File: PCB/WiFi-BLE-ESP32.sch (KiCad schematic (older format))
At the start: 27 parts, among them T1 1909763-1, U4 ESP32, U5 W25Q64FWSSIG, X3 FA-128_26.0000MF10Z-AC3

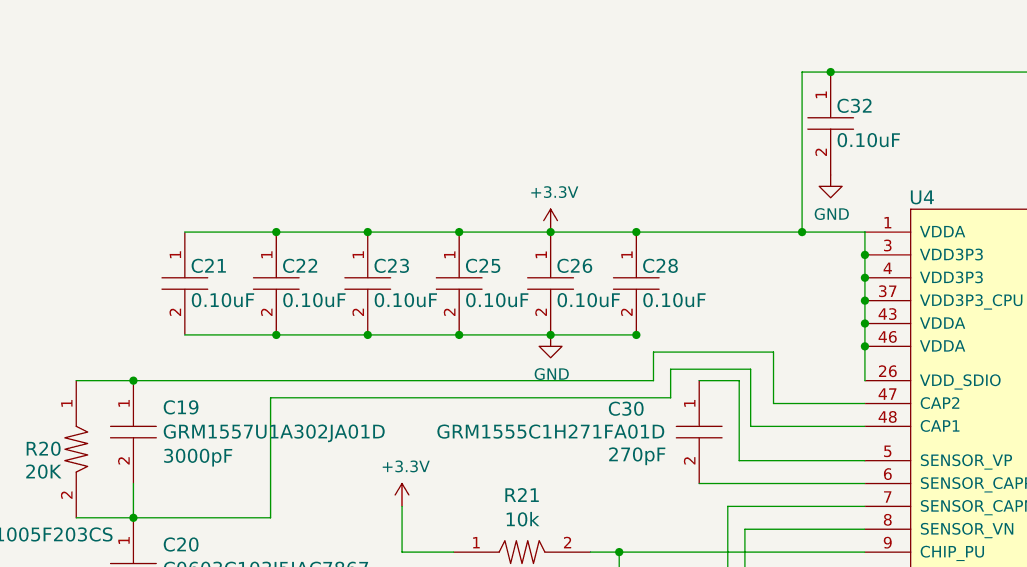
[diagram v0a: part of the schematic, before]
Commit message: Tweaking and ESP3212 version
Continuing to tweak the PCB, for optimal RF performance, thinking about
capping either the RF section of the MCU+RF entirely. Also made an
ESP3212 module version, both will be built at the same time when the
time comes.
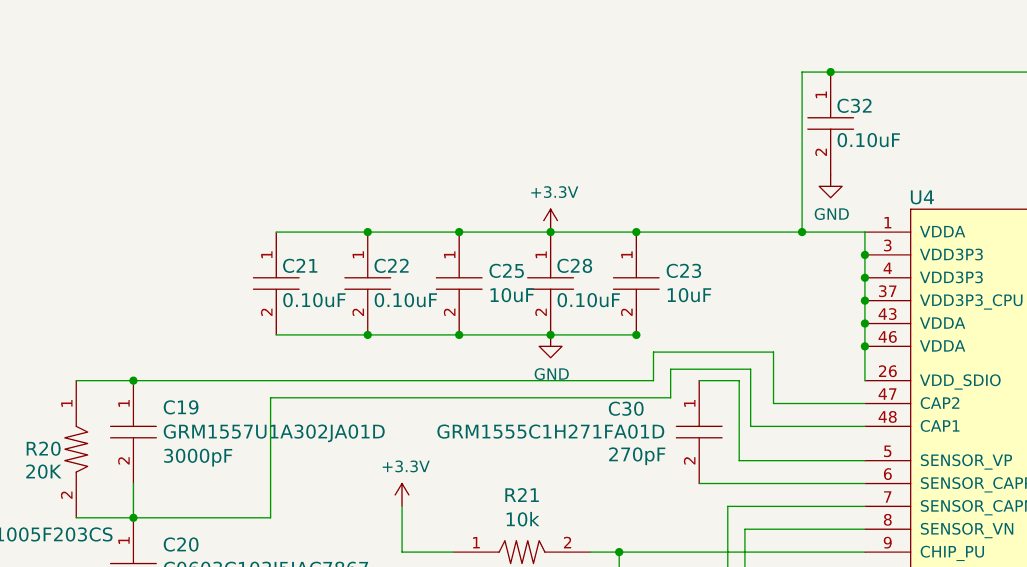
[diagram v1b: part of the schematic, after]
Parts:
- removed C23, C25, C26: CL05B104JP5NNNC, PCB_Footprints:C0402, symbol CL05B104JP5NNNC
- added C23, C25: CL10A106KQ8NNNC, PCB_Footprints:C0603, symbol CL10A106KQ8NNNC
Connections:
- net +3V3: now also C23.1, C25.1
- net GND: now also C23.2, C25.2
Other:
- moved on the sheet: C21, C22, C28

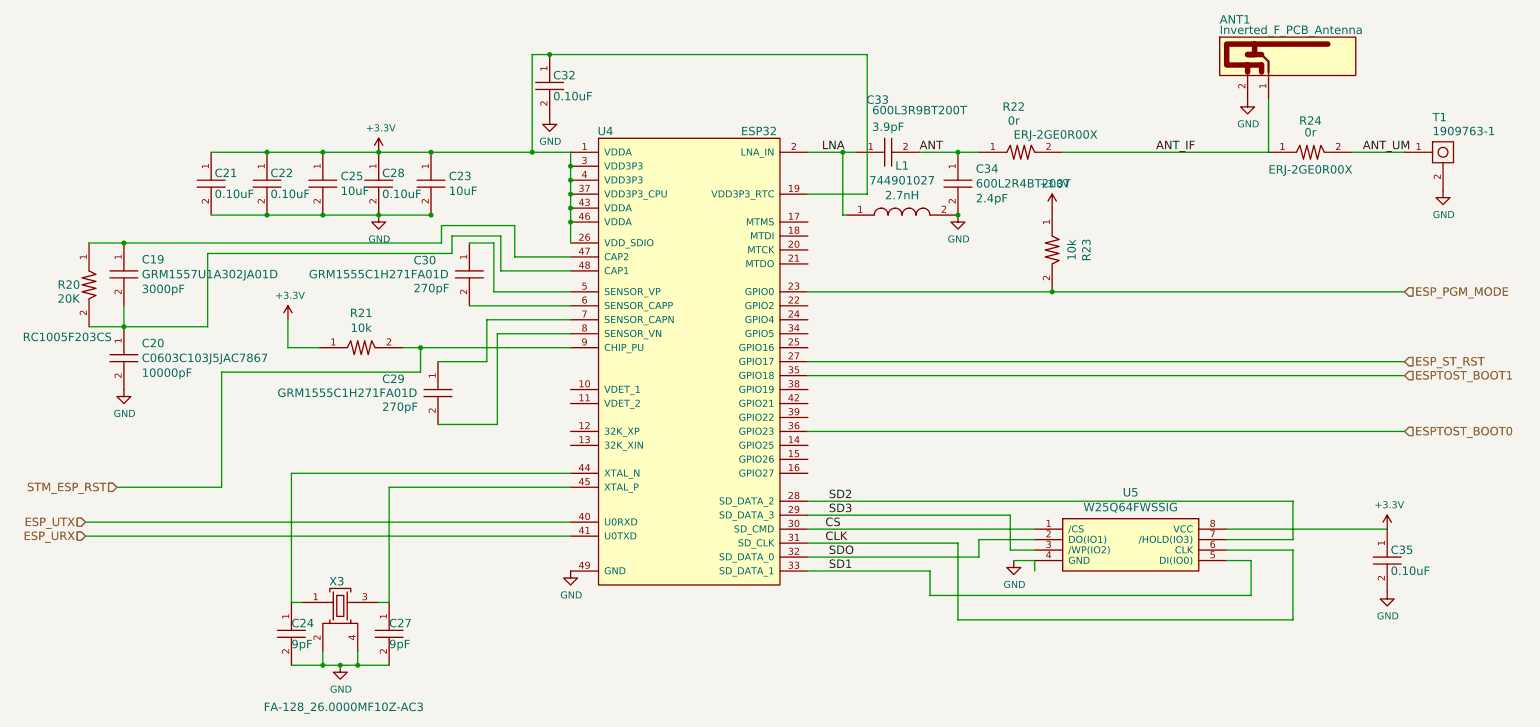
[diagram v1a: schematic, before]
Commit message: Tweaks, DRC cleared, images, readme
Tweaked both designs according to the dev board scheamtics provided by
Espressif in the datasheets folder. Cleared both boards of DRC
violations, added new images and updated the readme.
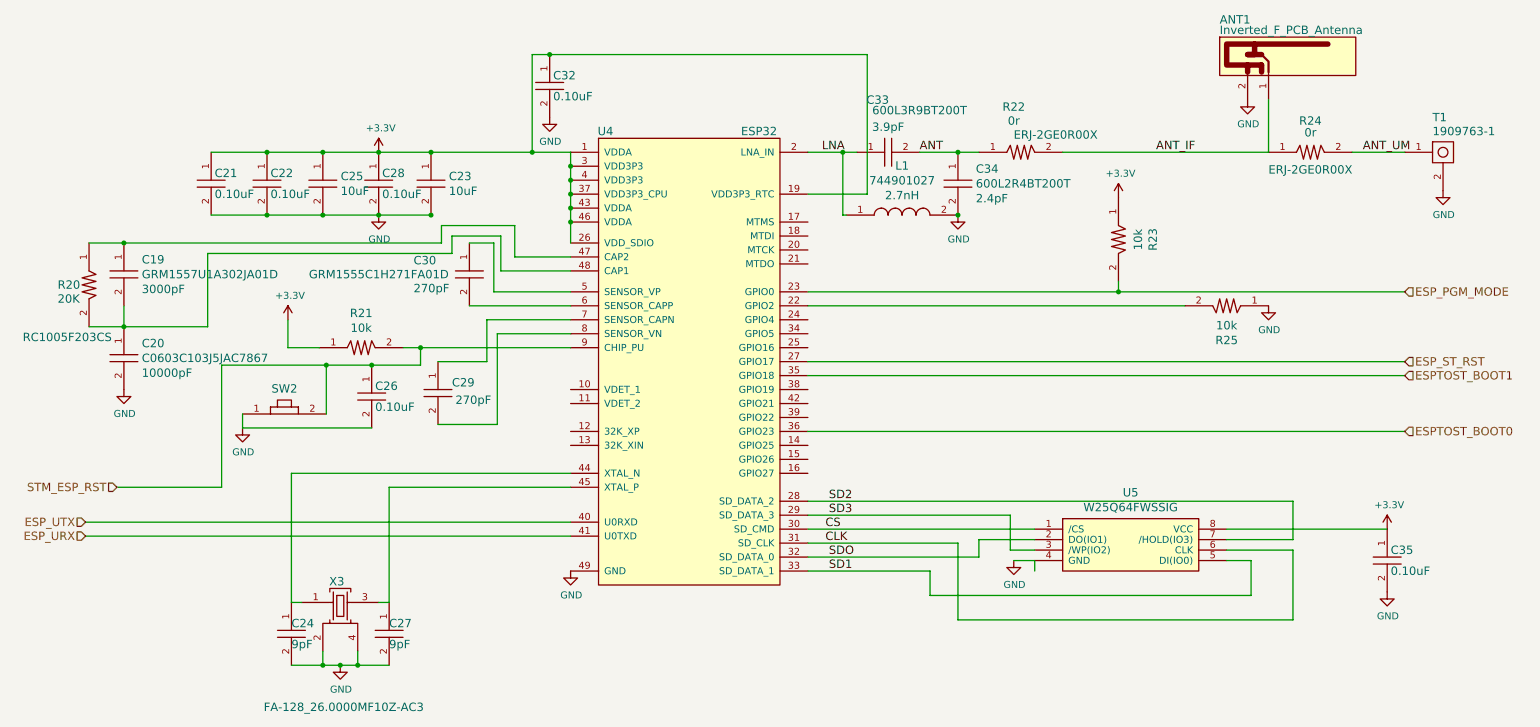
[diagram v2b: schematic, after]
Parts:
- added C26: CL05B104JP5NNNC, PCB_Footprints:C0402, symbol CL05B104JP5NNNC
- added R25: RC1005F103CS, PCB_Footprints:R0402, symbol RC1005F103CS
- added SW2: B3U-1000P, PCB_Footprints:B3U-1000P, symbol B3U-1000P
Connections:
- net GND: now also C26.2, R25.1, SW2.1
- net STM_ESP_RST: now also C26.1, SW2.2
- net at U4.22 (GPIO2): now also R25.2
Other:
- moved on the sheet: R23

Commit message: On/Off And Cleanup
Onoff Switch added, PCB extended 1mm to accomodated everything. routing
and traes cleaned up. Heat sinking ground pours added to the BQ chip
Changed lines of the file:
@@
 $EndComp
 $Comp
-L +3.3V #PWR40
+L +3.3V #PWR41
 U 1 1 57EA49BD
 P 3075 1950
-F 0 "#PWR40" H 3075 1800 50  0001 C CNN
+F 0 "#PWR41" H 3075 1800 50  0001 C CNN
 F 1 "+3.3V" H 3090 2123 50  0000 C CNN
 F 2 "" H 3075 1950 50  0000 C CNN
@@
 $EndComp
 $Comp
-L GND #PWR41
+L GND #PWR42
 U 1 1 57EA49DF
 P 3075 2400
-F 0 "#PWR41" H 3075 2150 50  0001 C CNN
+F 0 "#PWR42" H 3075 2150 50  0001 C CNN
 F 1 "GND" H 3080 2227 50  0000 C CNN
 F 2 "" H 3075 2400 50  0000 C CNN
@@
 $EndComp
 $Comp
-L GND #PWR43
+L GND #PWR44
 U 1 1 57EA4CD5
 P 4450 4950
-F 0 "#PWR43" H 4450 4700 50  0001 C CNN
+F 0 "#PWR44" H 4450 4700 50  0001 C CNN
 F 1 "GND" H 4455 4777 50  0000 C CNN
 F 2 "" H 4450 4950 50  0000 C CNN
@@
 $EndComp
 $Comp
-L +3.3V #PWR38
+L +3.3V #PWR39
 U 1 1 57EA52FC
 P 2425 3150
-F 0 "#PWR38" H 2425 3000 50  0001 C CNN
+F 0 "#PWR39" H 2425 3000 50  0001 C CNN
 F 1 "+3.3V" H 2440 3323 50  0000 C CNN
 F 2 "" H 2425 3150 50  0000 C CNN
@@
 $EndComp
 $Comp
-L GND #PWR39
+L GND #PWR40
 U 1 1 57EA84FC
 P 2800 5625
-F 0 "#PWR39" H 2800 5375 50  0001 C CNN
+F 0 "#PWR40" H 2800 5375 50  0001 C CNN
 F 1 "GND" H 2805 5452 50  0000 C CNN
 F 2 "" H 2800 5625 50  0000 C CNN
@@
 $EndComp
 $Comp
-L +3.3V #PWR46
+L +3.3V #PWR47
 U 1 1 5800AB01
 P 8375 2275
-F 0 "#PWR46" H 8375 2125 50  0001 C CNN
+F 0 "#PWR47" H 8375 2125 50  0001 C CNN
 F 1 "+3.3V" H 8390 2448 50  0000 C CNN
 F 2 "" H 8375 2275 50  0000 C CNN
@@
 $EndComp
 $Comp
-L +3.3V #PWR49
+L +3.3V #PWR50
 U 1 1 5800EACB
 P 10300 4650
-F 0 "#PWR49" H 10300 4500 50  0001 C CNN
+F 0 "#PWR50" H 10300 4500 50  0001 C CNN
 F 1 "+3.3V" H 10315 4823 50  0000 C CNN
 F 2 "" H 10300 4650 50  0000 C CNN
@@
 $EndComp
 $Comp
-L GND #PWR50
+L GND #PWR51
 U 1 1 5800EB03
 P 10300 5100
-F 0 "#PWR50" H 10300 4850 50  0001 C CNN
+F 0 "#PWR51" H 10300 4850 50  0001 C CNN
 F 1 "GND" H 10305 4927 50  0000 C CNN
 F 2 "" H 10300 5100 50  0000 C CNN
@@
 $EndComp
 $Comp
-L GND #PWR45
+L GND #PWR46
 U 1 1 5800EB4A
 P 7625 4875
-F 0 "#PWR45" H 7625 4625 50  0001 C CNN
+F 0 "#PWR46" H 7625 4625 50  0001 C CNN
 F 1 "GND" H 7630 4702 50  0000 C CNN
 F 2 "" H 7625 4875 50  0000 C CNN
@@
 $EndComp
 $Comp
-L GND #PWR42
+L GND #PWR43
 U 1 1 5800EFA0
 P 4300 1700
-F 0 "#PWR42" H 4300 1450 50  0001 C CNN
+F 0 "#PWR43" H 4300 1450 50  0001 C CNN
 F 1 "GND" H 4305 1527 50  0000 C CNN
 F 2 "" H 4300 1700 50  0000 C CNN
@@
 $EndComp
 $Comp
-L GND #PWR47
+L GND #PWR48
 U 1 1 58010E09
 P 9300 1575
-F 0 "#PWR47" H 9300 1325 50  0001 C CNN
+F 0 "#PWR48" H 9300 1325 50  0001 C CNN
 F 1 "GND" H 9305 1402 50  0000 C CNN
 F 2 "" H 9300 1575 50  0000 C CNN
@@
 $EndComp
 $Comp
-L GND #PWR51
+L GND #PWR52
 U 1 1 58010F40
 P 10700 2225
-F 0 "#PWR51" H 10700 1975 50  0001 C CNN
+F 0 "#PWR52" H 10700 1975 50  0001 C CNN
 F 1 "GND" H 10705 2052 50  0000 C CNN
 F 2 "" H 10700 2225 50  0000 C CNN
@@
 $EndComp
 $Comp
-L GND #PWR36
+L GND #PWR37
 U 1 1 5802DE2F
 P 1250 3650
-F 0 "#PWR36" H 1250 3400 50  0001 C CNN
+F 0 "#PWR37" H 1250 3400 50  0001 C CNN
 F 1 "GND" H 1255 3477 50  0000 C CNN
 F 2 "" H 1250 3650 50  0000 C CNN
@@
 LNA
 $Comp
-L GND #PWR44
+L GND #PWR45
 U 1 1 5802EBA7
 P 7225 2400
-F 0 "#PWR44" H 7225 2150 50  0001 C CNN
+F 0 "#PWR45" H 7225 2150 50  0001 C CNN
 F 1 "GND" H 7230 2227 50  0000 C CNN
 F 2 "" H 7225 2400 50  0000 C CNN
@@
 $EndComp
 Wire Wire Line
-	1875 1950 2275 1950
-Wire Wire Line
-	2275 1950 2675 1950
-Wire Wire Line
-	2675 1950 3075 1950
-Wire Wire Line
-	3075 1950 3450 1950
-Wire Wire Line
-	3450 1950 4175 1950
-Wire Wire Line
-	4175 1950 4450 1950
+	1875 1950 4450 1950
 Connection ~ 2275 1950
 Connection ~ 2675 1950
@@
 Connection ~ 3075 1950
 Wire Wire Line
-	1875 2400 2275 2400
-Wire Wire Line
-	2275 2400 2675 2400
-Wire Wire Line
-	2675 2400 3075 2400
-Wire Wire Line
-	3075 2400 3450 2400
+	1875 2400 3450 2400
 Connection ~ 2275 2400
 Connection ~ 2675 2400
@@
 Connection ~ 3450 2400
 Wire Wire Line
-	4450 1950 4450 2050
-Wire Wire Line
-	4450 2050 4450 2150
-Wire Wire Line
-	4450 2150 4450 2250
-Wire Wire Line
-	4450 2250 4450 2350
-Wire Wire Line
-	4450 2350 4450 2450
-Wire Wire Line
-	4450 2450 4450 2600
+	4450 1950 4450 2600
 Connection ~ 4450 2350
 Connection ~ 4450 2250
@@
 Connection ~ 4450 2050
 Wire Wire Line
-	3250 3350 3375 3350
-Wire Wire Line
-	3375 3350 4450 3350
+	3250 3350 4450 3350
 Wire Wire Line
 	2425 3150 2425 3350
@@
 	2450 5175 2525 5175
 Wire Wire Line
-	2450 5625 2675 5625
-Wire Wire Line
-	2675 5625 2800 5625
-Wire Wire Line
-	2800 5625 2925 5625
-Wire Wire Line
-	2925 5625 3150 5625
+	2450 5625 3150 5625
 Wire Wire Line
 	2675 5625 2675 5525
@@
 	4450 4700 975  4700
 Wire Wire Line
-	6150 2950 8375 2950
-Wire Wire Line
-	8375 2950 10425 2950
+	6150 2950 10425 2950
 Connection ~ 8375 2950
 Wire Wire Line
@@
 	6575 2250 6575 1250
 Wire Wire Line
-	6575 1250 4300 1250
-Wire Wire Line
-	4300 1250 4175 1250
+	6575 1250 4175 1250
 Wire Wire Line
 	4175 1250 4175 1950
@@
 	1850 2675 1850 3200
 Wire Wire Line
-	1850 3200 1250 3200
-Wire Wire Line
-	1250 3200 1000 3200
+	1850 3200 1000 3200
 Wire Wire Line
 	4450 2700 4050 2700
@@
 	3525 2475 3525 2600
 Wire Wire Line
-	3525 2600 1250 2600
-Wire Wire Line
-	1250 2600 1000 2600
+	3525 2600 1000 2600
 Wire Wire Line
 	1250 3050 1250 3200
 Connection ~ 1250 3200
 Wire Wire Line
-	6950 1950 7225 1950
-Wire Wire Line
-	7225 1950 7375 1950
-Wire Wire Line
-	6150 1950 6400 1950
-Wire Wire Line
-	6400 1950 6500 1950
+	6950 1950 7375 1950
+Wire Wire Line
+	6150 1950 6500 1950
 Connection ~ 7225 1950
 Connection ~ 7225 2400
@@
 	8375 2875 8375 2950
 Wire Wire Line
-	8850 3050 8850 3050
-Wire Wire Line
-	8850 3050 6150 3050
+	6150 3050 8850 3050
 $Comp
 L B3U-1000P SW2
@@
 	3375 3475 3375 3350
 Wire Wire Line
-	1950 3475 2700 3475
-Wire Wire Line
-	2700 3475 3025 3475
-Wire Wire Line
-	3025 3475 3375 3475
+	1950 3475 3375 3475
 Wire Wire Line
 	2700 3475 2700 3825
 $Comp
-L GND #PWR37
+L GND #PWR38
 U 1 1 58076D0F
 P 2100 3925
-F 0 "#PWR37" H 2100 3675 50  0001 C CNN
+F 0 "#PWR38" H 2100 3675 50  0001 C CNN
 F 1 "GND" H 2105 3752 50  0000 C CNN
 F 2 "" H 2100 3925 50  0000 C CNN
@@
 Connection ~ 2700 3475
 $Comp
-L GND #PWR48
+L GND #PWR49
 U 1 1 5807A228
 P 9450 3050
-F 0 "#PWR48" H 9450 2800 50  0001 C CNN
+F 0 "#PWR49" H 9450 2800 50  0001 C CNN
 F 1 "GND" H 9455 2877 50  0000 C CNN
 F 2 "" H 9450 3050 50  0000 C CNN
